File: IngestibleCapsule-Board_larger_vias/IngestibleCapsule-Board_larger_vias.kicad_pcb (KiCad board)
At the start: 2 copper layers, 15 x 55 mm, 52 parts, among them J1 TC2030-NL, J2 AXF6K0412A, J3 AXF5K0412A, J4 513389873, J5 559099872, J6 Conn_01x02_Pin, U1 STM32G473CCUx, U2 MLX90640, U3 ADXL343, U4 W25Q16JVSS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

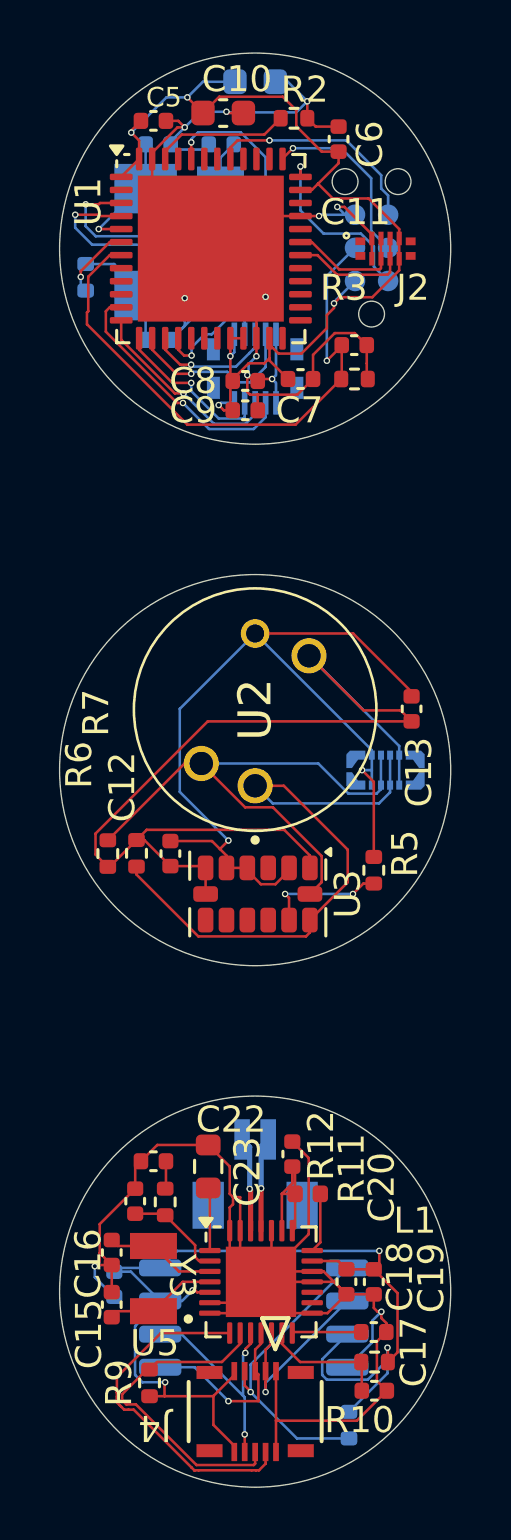
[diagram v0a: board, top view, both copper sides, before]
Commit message: larger vias implemented
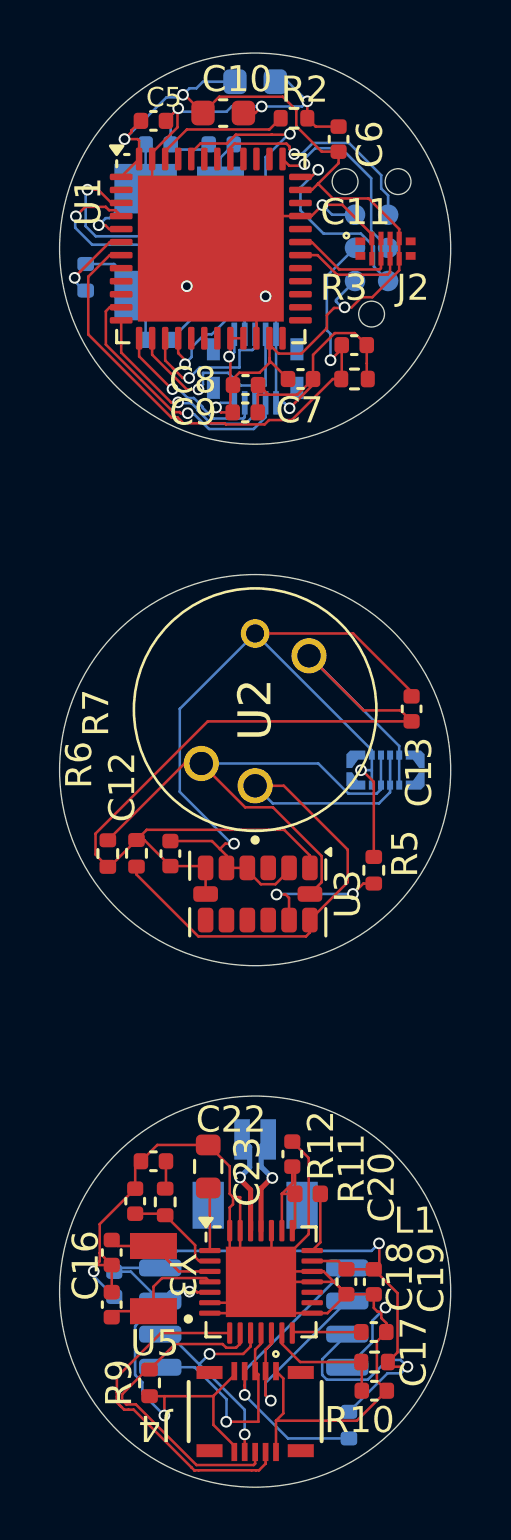
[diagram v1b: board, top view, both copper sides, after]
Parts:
- moved C8 0.16 mm to (99.6, 80.2)
- moved C9 0.08 mm to (99.6, 81.3)
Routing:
- net SPI_VDD: track 42.4 -> 44.3 mm
- net +3.3V: track 40.4 -> 42.2 mm
- net /SPI_MOSI: track 7.11 -> 8.70 mm
- net /Processor/LED_OUT: track 5.14 -> 6.66 mm
- net GND: track 52.8 -> 54.3 mm, vias 10 -> 7
- net /MCU_SPI_MISO: track 6.87 -> 8.23 mm
- net /MCU_SPI_MOSI: track 4.97 -> 5.96 mm
- net /SPI_MISO: track 7.14 -> 7.97 mm
- net SPI_GND: track 61.4 -> 62.1 mm
- net Net-(U1-PC14): track 10.0 -> 10.7 mm
- net Net-(U5-XTAL_C2): track 4.32 -> 4.99 mm
- net Net-(U3-SDO/ADDR): track 4.63 -> 5.29 mm
- net /Processor/SWDIO: track 7.02 -> 7.57 mm
- net I2C_GND: track 34.9 -> 35.4 mm
- net /MCU_MEM_CS: track 4.39 -> 4.89 mm
